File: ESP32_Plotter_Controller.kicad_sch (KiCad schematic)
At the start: 53 parts, among them J1 Power, J10 Micro_SD_Card_TF-01A, J11 Neo Pixel LEDs, J12 Pen Direction, J13 ARM JTAG 10pin, J14 Y Limit, J15 X Limit, J16 Pen Lift, J17 Vselect, J18 Y Motor, J19 X Motor, J2 5V Aux, J3 USB_C_Receptacle_USB2.0, J4 Vin Aux, J5 E-Stop, J6 Aux Port (SPI), J7 Aux Port (I2C), J8 X Limit Switch, J9 Y Limit Switch, SW1 RESET, SW2 BOOT, U1 ESP32-WROOM-32D, U2 CH340C, U3 XL1509, U4 AMS1117-3.3

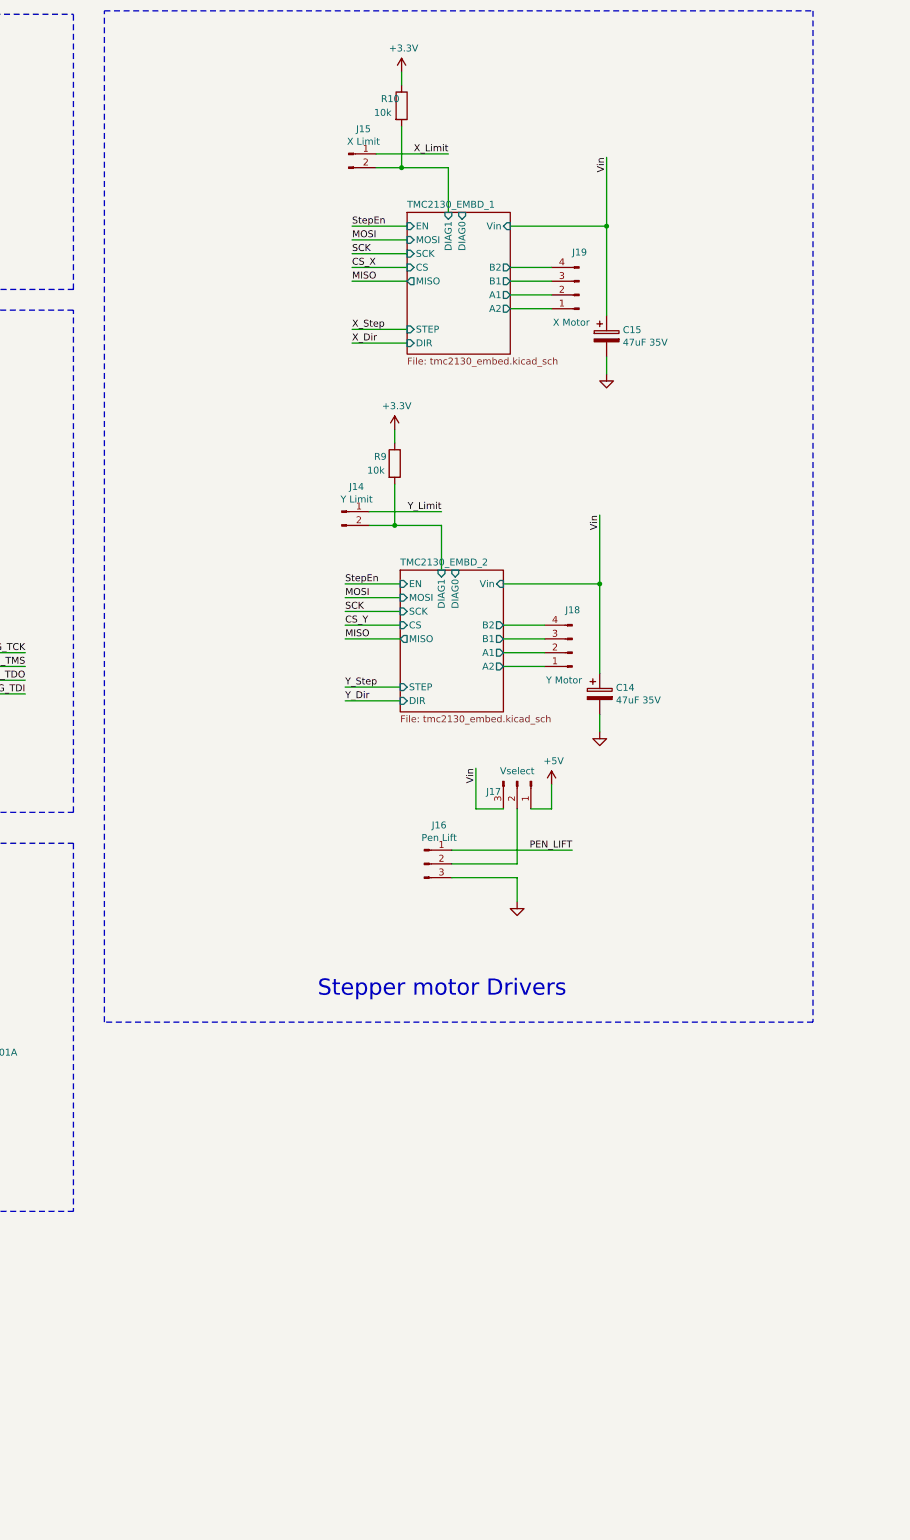
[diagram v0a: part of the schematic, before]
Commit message: Might as well add a z motor stepper driver at this stage
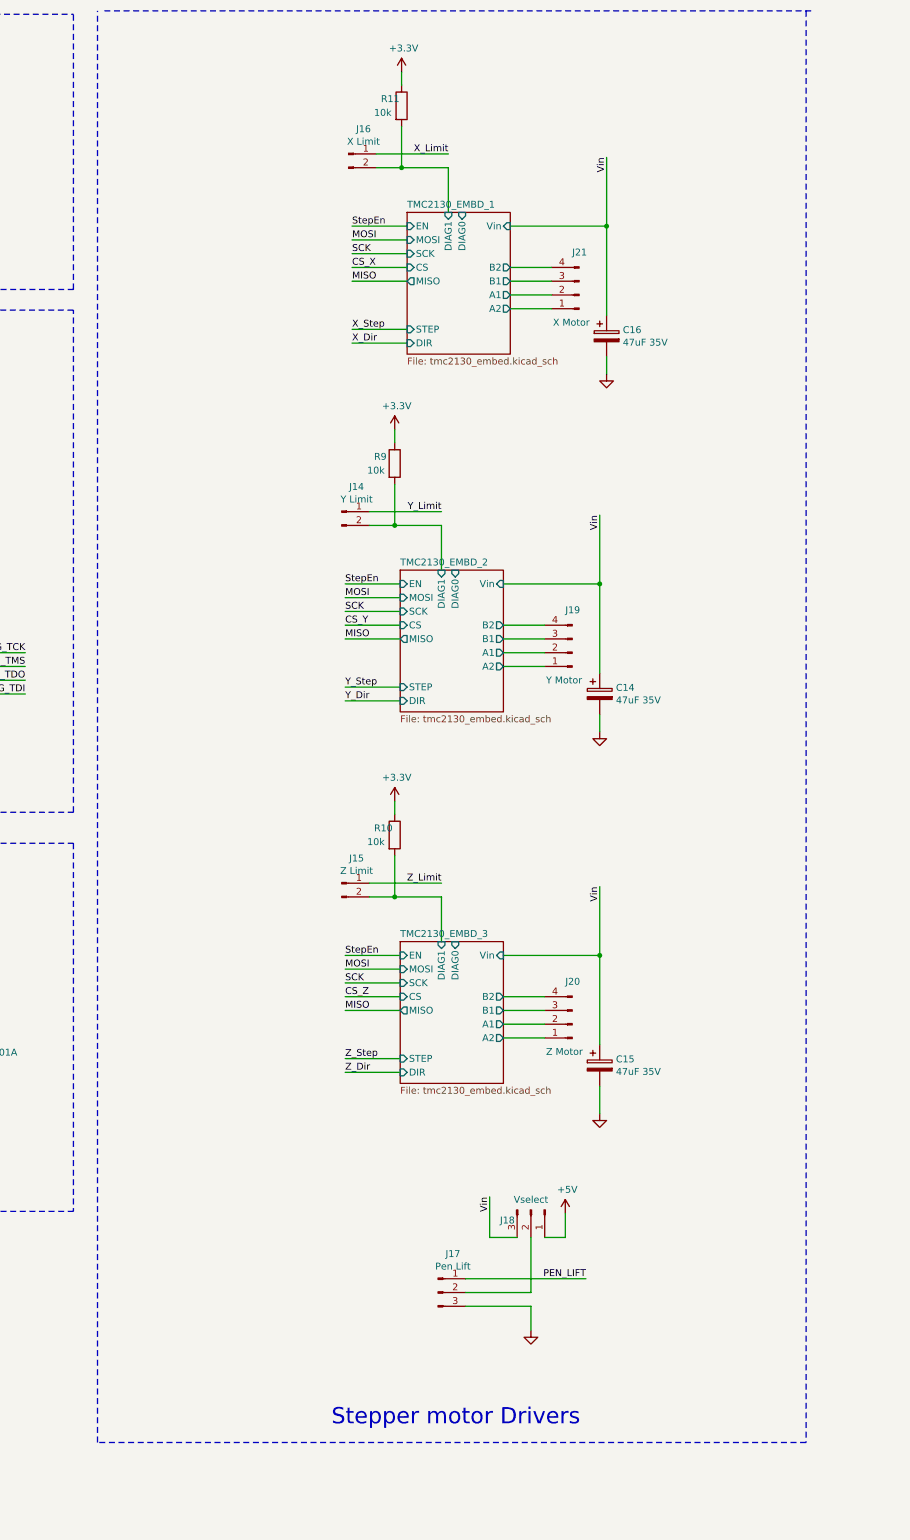
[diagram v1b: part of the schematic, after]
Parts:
- added C15: 47uF 35V, Capacitor_SMD:CP_Elec_6.3x5.7, symbol Device:CP
- added J15: Z Limit, Connector_PinHeader_2.54mm:PinHeader_1x02_P2.54mm_Vertical, symbol Connector:Conn_01x02_Male
- added J20: Z Motor, Connector_JST:JST_PH_S4B-PH-K_1x04_P2.00mm_Horizontal, symbol Connector:Conn_01x04_Male
- added R10: 10k, Resistor_SMD:R_0603_1608Metric, symbol Device:R
- renumbered C15 to C16, J15 to J16, J16 to J17, J17 to J18, J18 to J19, J19 to J21, R10 to R11
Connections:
- net +3.3V: now also R10.1
- net GND: now also C15.2
- net Vin: now also C15.1
- new net TMC2130_EMBD_3/A1: J20.2 (Pin_2)
- new net TMC2130_EMBD_3/A2: J20.1 (Pin_1)
- new net TMC2130_EMBD_3/B1: J20.3 (Pin_3)
- new net TMC2130_EMBD_3/B2: J20.4 (Pin_4)
- new net TMC2130_EMBD_3/DIAG1: J15.2 (Pin_2), R10.2
- new net Z_Limit: J15.1 (Pin_1)
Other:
- added sheet TMC2130_EMBD_3 (tmc2130_embed.kicad_sch)
- moved on the sheet: J17, J18

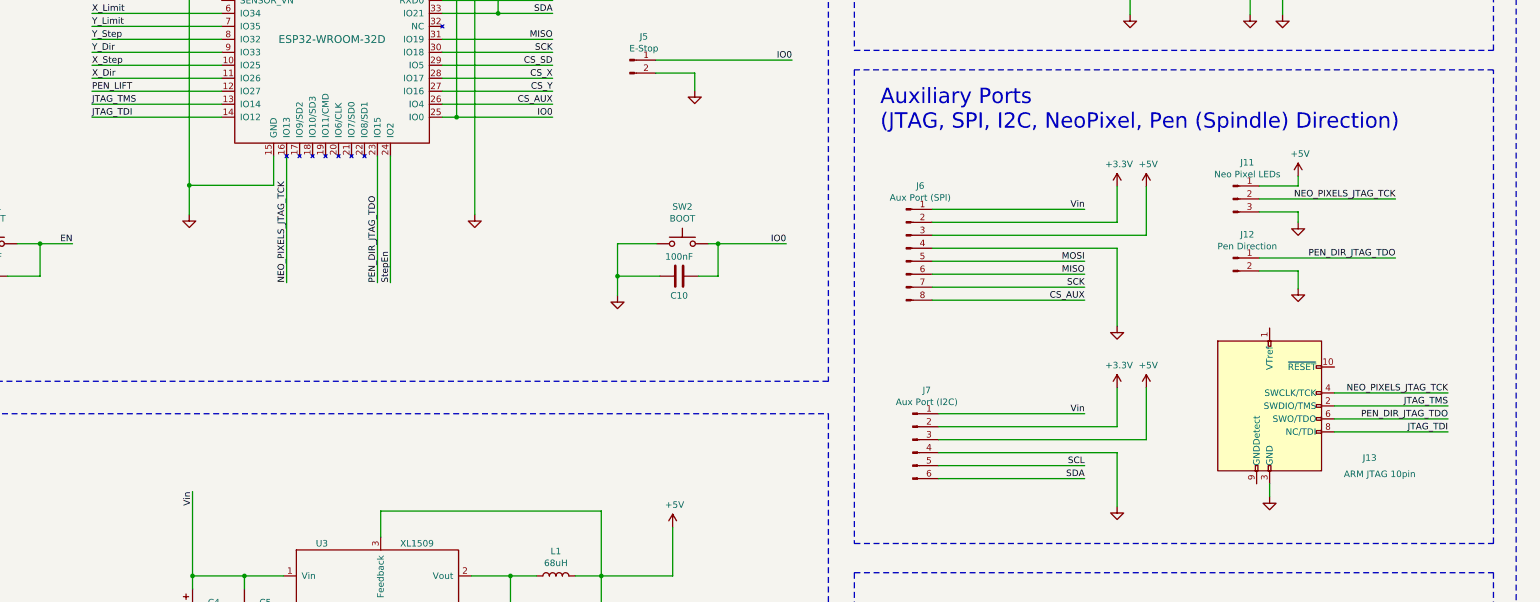
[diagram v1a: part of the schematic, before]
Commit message: Assign JTAG pins to Z stepper driver. Remove JTAG, Pen Direction and Neo Pixel ports
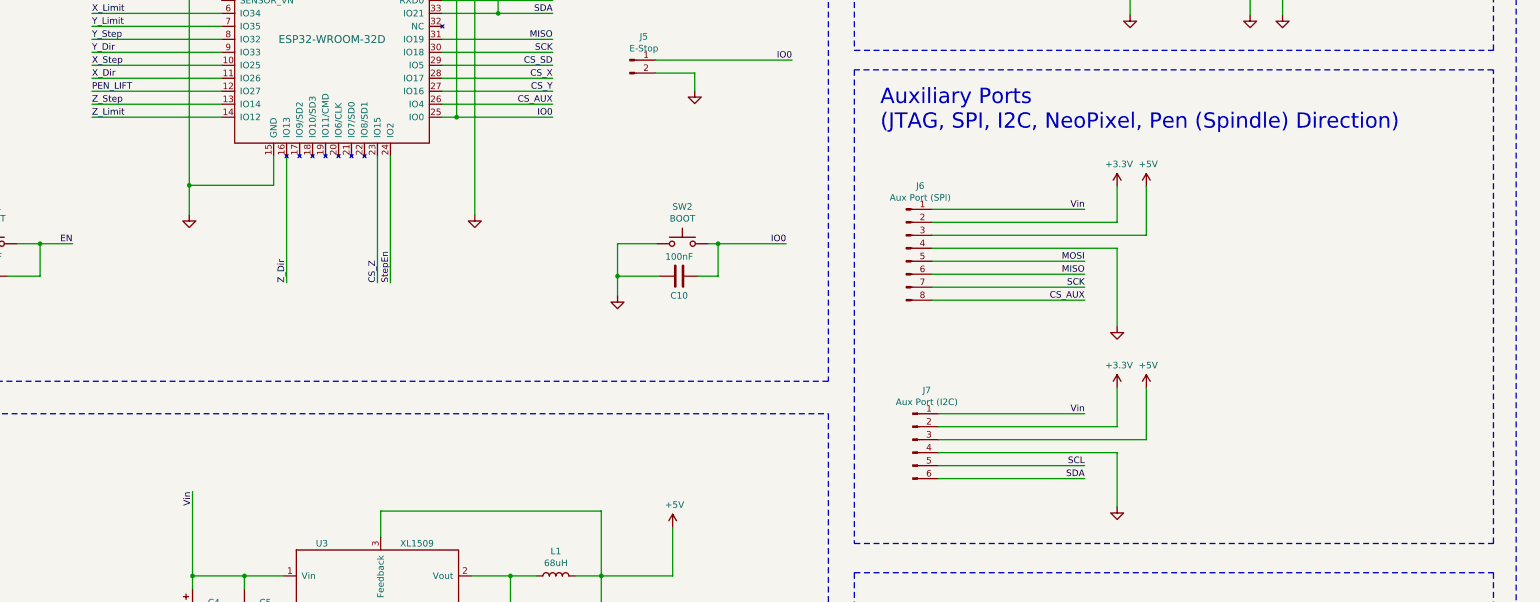
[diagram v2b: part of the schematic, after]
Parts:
- removed J11: Neo Pixel LEDs, Connector_JST:JST_PH_S3B-PH-K_1x03_P2.00mm_Horizontal, symbol Connector:Conn_01x03_Male
- removed J12: Pen Direction, Connector_JST:JST_PH_S2B-PH-K_1x02_P2.00mm_Horizontal, symbol Connector:Conn_01x02_Male
- removed J13: ARM JTAG 10pin, Connector_PinSocket_2.54mm:PinSocket_2x05_P2.54mm_Vertical, symbol Connector:Conn_ARM_JTAG_SWD_10
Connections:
- net JTAG_TDI is gone; now on net Z_Limit: U1.14 (IO12)
- net JTAG_TMS is gone; now on net Z_Step: U1.13 (IO14)
- net NEO_PIXELS_JTAG_TCK is gone; now on net Z_Dir: U1.16 (IO13)
- net PEN_DIR_JTAG_TDO is gone; now on net CS_Z: U1.23 (IO15)

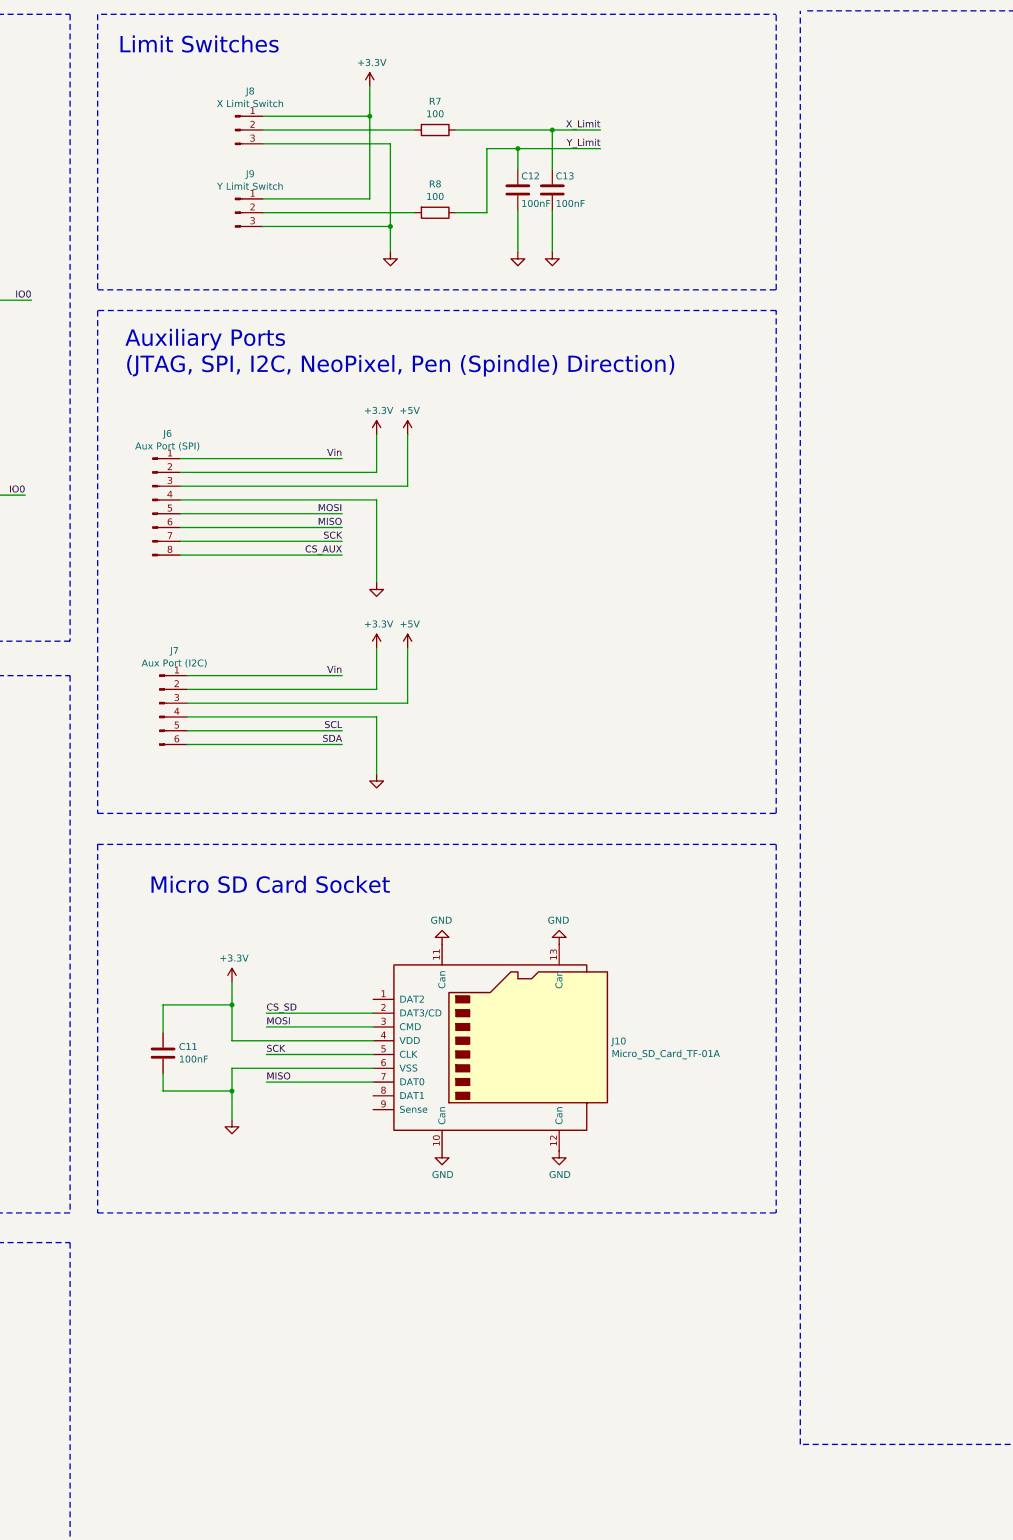
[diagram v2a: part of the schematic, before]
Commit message: All components placed - first pass
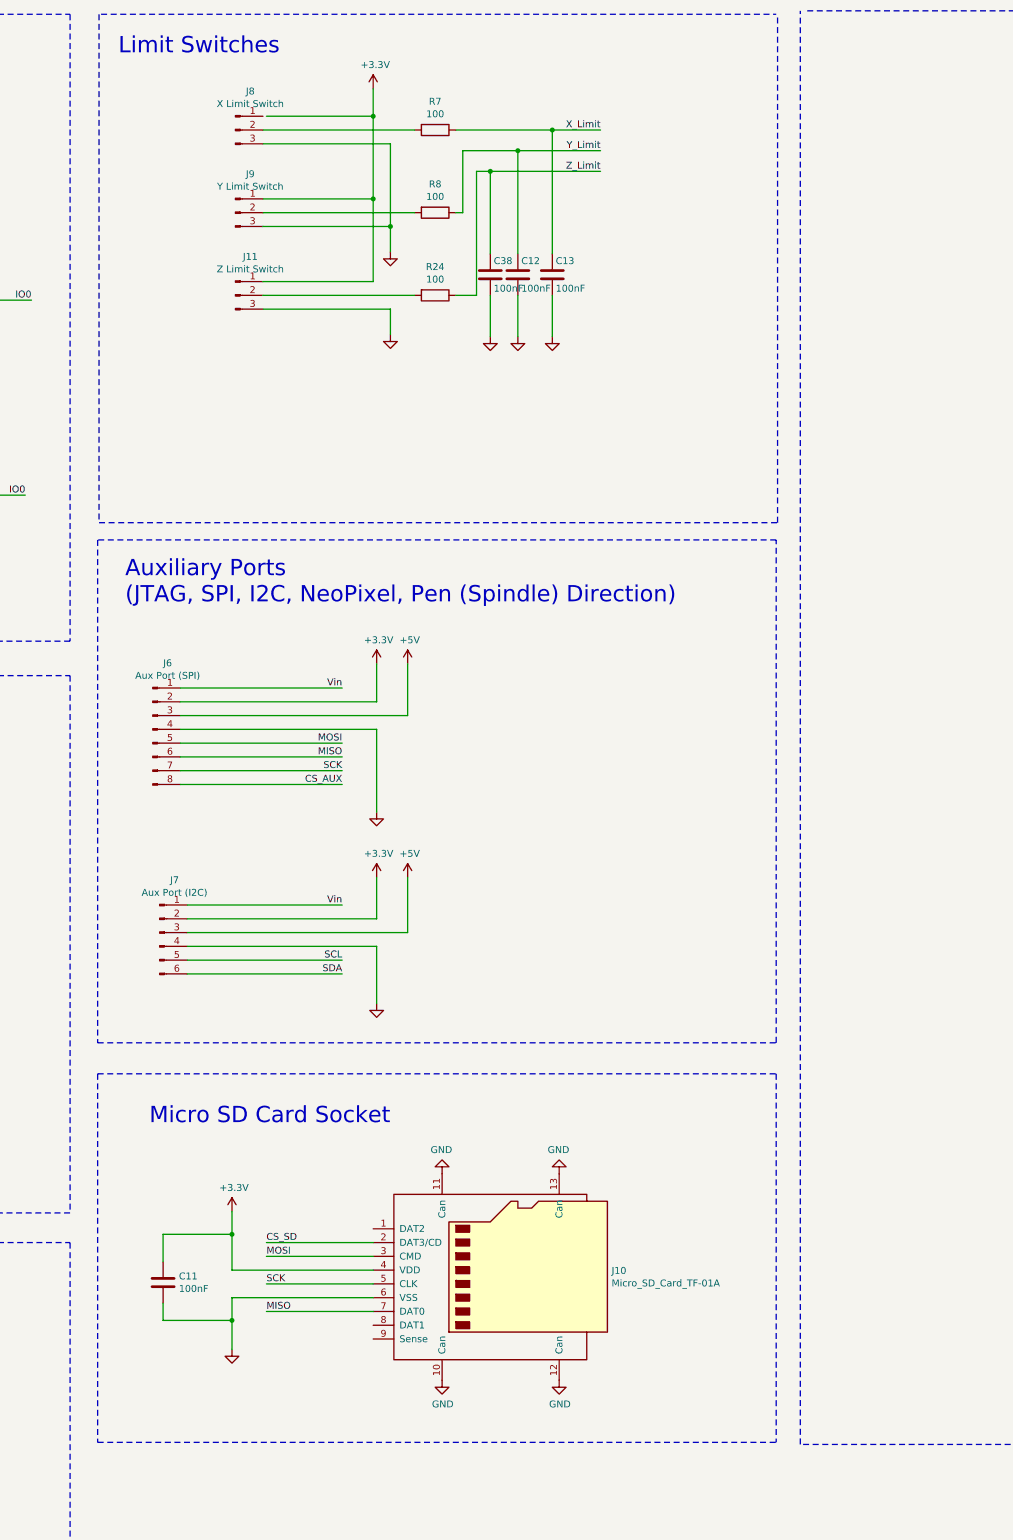
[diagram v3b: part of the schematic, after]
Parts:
- added C38: 100nF, Capacitor_SMD:C_0603_1608Metric, symbol Device:C
- added J11: Z Limit Switch, Connector_JST:JST_PH_S3B-PH-K_1x03_P2.00mm_Horizontal, symbol Connector:Conn_01x03_Male
- added R24: 100, Resistor_SMD:R_0603_1608Metric, symbol Device:R
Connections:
- net +3.3V: now also J11.1 (Pin_1); no longer J8.1 (Pin_1)
- net GND: now also C38.2, J11.3 (Pin_3)
- net Z_Limit: now also C38.1, R24.1
- new net: J11.2 (Pin_2), R24.2
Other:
- moved on the sheet: C11, C12, C13, J10, J6, J7
